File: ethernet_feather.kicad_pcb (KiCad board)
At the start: 4 copper layers, 48 parts, among them J1 USB_C_Receptacle_USB2.0, J2 TC2030-NL, J3 Conn_01x02_MountingPin, J4 RJ45_Abracon_ARJM11D7-114-AB-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, J5 Conn_02x02_Odd_Even, U1 MIMXRT1051CVJ5B, U2 LP3982IMM-3.3, U3 MCP73831-2-OT, U4 W25Q32JVZP, U5 WE-TVS-82400102, Y1 24MHz 6pF, Y2 32.768kHz 7pF

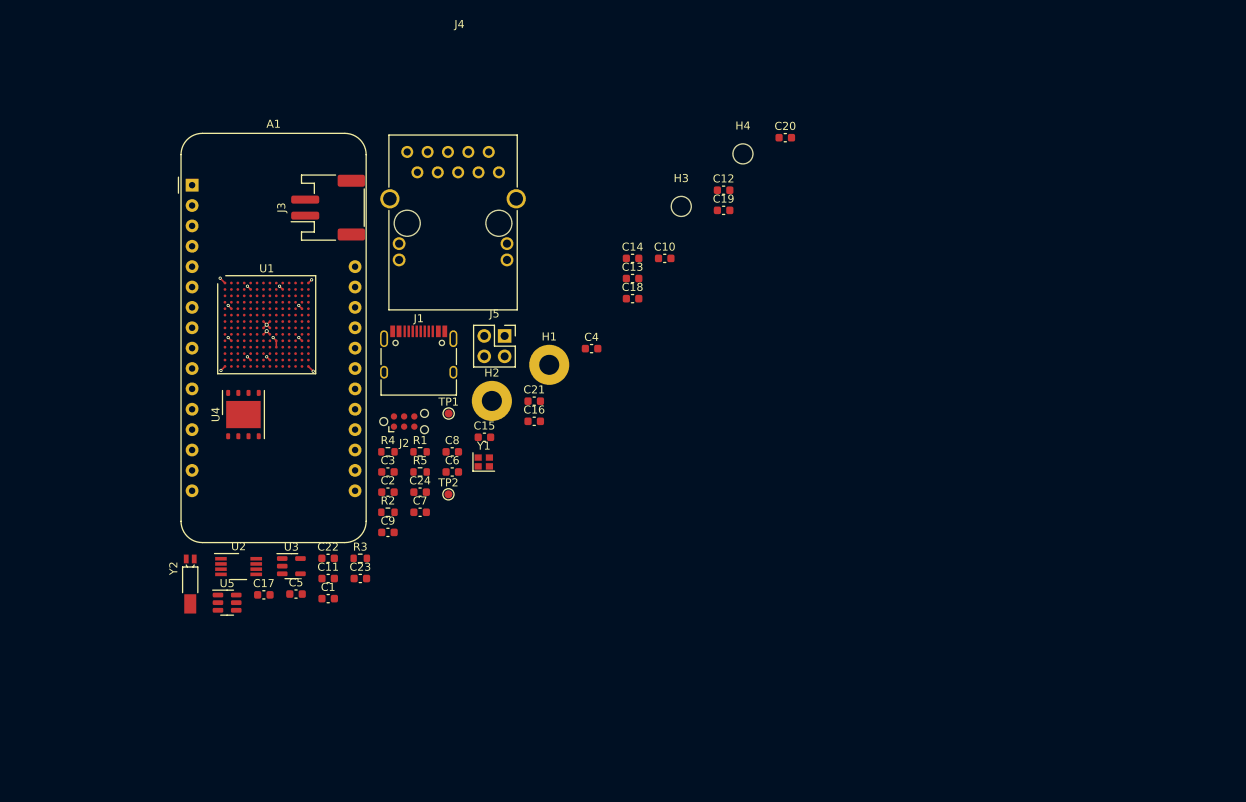
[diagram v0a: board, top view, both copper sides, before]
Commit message: Add microSD card and annotate mostly complete schematic
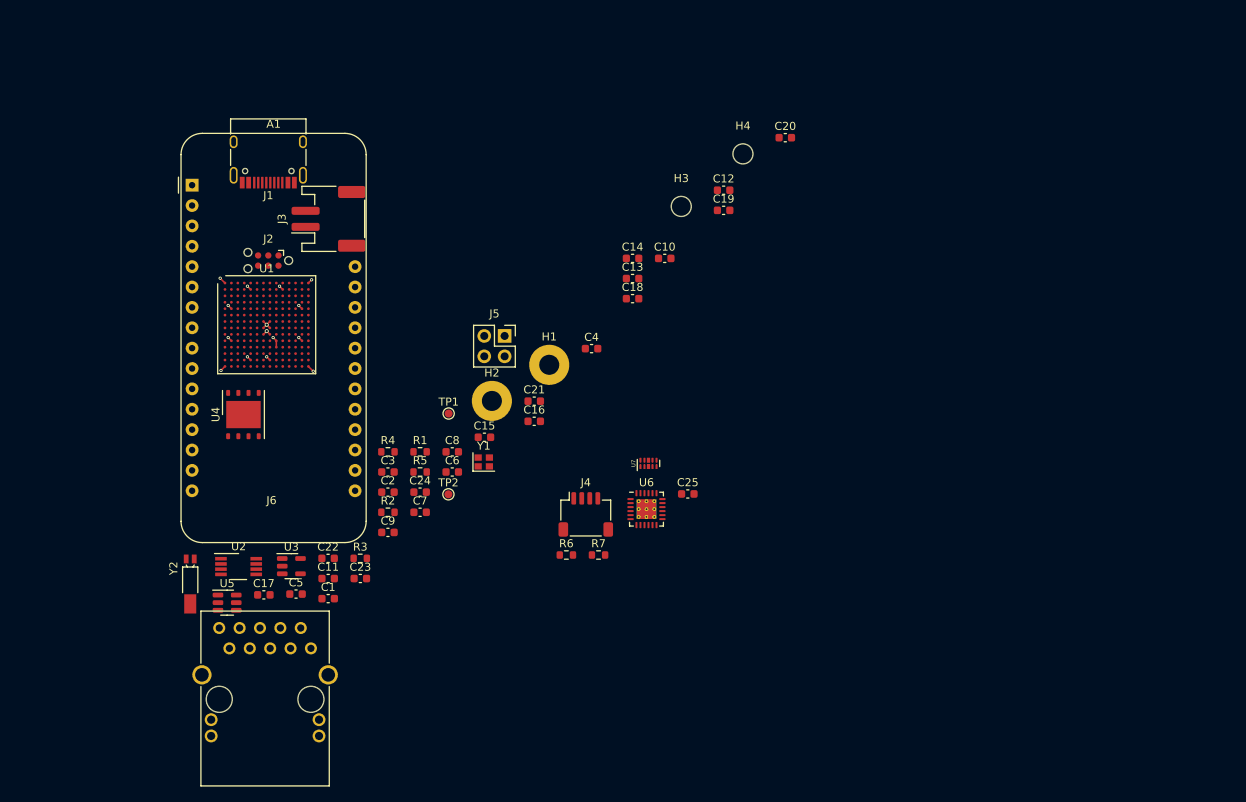
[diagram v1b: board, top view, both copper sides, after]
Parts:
- added C25: 100nF, Capacitor_SMD:C_0603_1608Metric, F.Cu at (151.6, 113.2)
- added J4: JST SH4 pin, Connector_JST:JST_SH_SM04B-SRSS-TB_1x04-1MP_P1.00mm_Horizontal, F.Cu at (138.9, 115.8)
- added R6: 10kΩ, Resistor_SMD:R_0603_1608Metric, F.Cu at (136.5, 120.8)
- added R7: 10kΩ, Resistor_SMD:R_0603_1608Metric, F.Cu at (140.5, 120.8)
- added U6: LAN8742A, Package_DFN_QFN:VQFN-24-1EP_4x4mm_P0.5mm_EP2.45x2.45mm_ThermalVias, F.Cu at (146.4, 115.1)
- added U7: HSP061-4M10, ethernet_feather:ST_µQFN-10L, F.Cu at (146.7, 109.4)
- J3: value Conn_01x02_MountingPin -> JST PH 2 pin
- moved J6 63.8 mm to (98.9, 138.8)
- moved J1 32.6 mm to (99.3, 70.3), turned to 180 degrees
- moved J2 26.3 mm to (99.3, 84.1), turned to 180 degrees
- moved J3 1.40 mm to (106.8, 78.9)
- renumbered J4 to J6
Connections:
- A1 pad 1: unconnected-(A1-Pad1) -> (no net)
- A1 pad 10: unconnected-(A1-Pad10) -> (no net)
- A1 pad 11: unconnected-(A1-Pad11) -> (no net)
- A1 pad 12: unconnected-(A1-Pad12) -> (no net)
- A1 pad 13: unconnected-(A1-Pad13) -> (no net)
- A1 pad 14: unconnected-(A1-Pad14) -> (no net)
- A1 pad 15: unconnected-(A1-Pad15) -> (no net)
- A1 pad 16: unconnected-(A1-Pad16) -> (no net)
- A1 pad 17: unconnected-(A1-Pad17) -> (no net)
- A1 pad 18: unconnected-(A1-Pad18) -> (no net)
- A1 pad 19: unconnected-(A1-Pad19) -> (no net)
- A1 pad 2: unconnected-(A1-Pad2) -> (no net)
- A1 pad 20: unconnected-(A1-Pad20) -> (no net)
- A1 pad 21: unconnected-(A1-Pad21) -> (no net)
- A1 pad 22: unconnected-(A1-Pad22) -> (no net)
- A1 pad 23: unconnected-(A1-Pad23) -> (no net)
- A1 pad 24: unconnected-(A1-Pad24) -> (no net)
- A1 pad 25: unconnected-(A1-Pad25) -> (no net)
- A1 pad 26: unconnected-(A1-Pad26) -> (no net)
- A1 pad 27: unconnected-(A1-Pad27) -> (no net)
- A1 pad 28: unconnected-(A1-Pad28) -> (no net)
- A1 pad 3: unconnected-(A1-Pad3) -> (no net)
- A1 pad 4: unconnected-(A1-Pad4) -> (no net)
- A1 pad 5: unconnected-(A1-Pad5) -> (no net)
- A1 pad 6: unconnected-(A1-Pad6) -> (no net)
- A1 pad 7: unconnected-(A1-Pad7) -> (no net)
- A1 pad 8: unconnected-(A1-Pad8) -> (no net)
- A1 pad 9: unconnected-(A1-Pad9) -> (no net)
- C5 pad 1: unconnected-(C5-Pad1) -> (no net)
- C5 pad 2: unconnected-(C5-Pad2) -> (no net)
- J1 pad A8: unconnected-(J1-PadA8) -> (no net)
- J1 pad B8: unconnected-(J1-PadB8) -> (no net)
- J2 pad 4: /SWCLK -> (no net)
- J6 pad 10: unconnected-(J4-Pad10) -> /ENET_TX+
- J6 pad 11: unconnected-(J4-Pad11) -> (no net)
- J6 pad 12: unconnected-(J4-Pad12) -> (no net)
- J6 pad 13: unconnected-(J4-Pad13) -> (no net)
- J6 pad 14: unconnected-(J4-Pad14) -> (no net)
- J6 pad 3: unconnected-(J4-Pad3) -> /ENET_RX-
- J6 pad 5: unconnected-(J4-Pad5) -> /ENET_RX+
- J6 pad 8: unconnected-(J4-Pad8) -> /ENET_TX-
- U1 pad A11: unconnected-(U1-PadA11) -> (no net)
- U1 pad A12: unconnected-(U1-PadA12) -> (no net)
- U1 pad A13: unconnected-(U1-PadA13) -> (no net)
- U1 pad A2: unconnected-(U1-PadA2) -> (no net)
- U1 pad A3: unconnected-(U1-PadA3) -> (no net)
- U1 pad A4: unconnected-(U1-PadA4) -> (no net)
- U1 pad A5: unconnected-(U1-PadA5) -> (no net)
- U1 pad A6: unconnected-(U1-PadA6) -> (no net)
- U1 pad A7: unconnected-(U1-PadA7) -> (no net)
- U1 pad A9: /SWDCLK -> (no net)
- U1 pad B1: unconnected-(U1-PadB1) -> (no net)
- U1 pad B11: unconnected-(U1-PadB11) -> (no net)
- U1 pad B12: unconnected-(U1-PadB12) -> (no net)
- U1 pad B13: unconnected-(U1-PadB13) -> (no net)
- U1 pad B14: unconnected-(U1-PadB14) -> (no net)
- U1 pad B2: unconnected-(U1-PadB2) -> (no net)
- U1 pad B3: unconnected-(U1-PadB3) -> (no net)
- U1 pad B4: unconnected-(U1-PadB4) -> (no net)
- U1 pad B6: unconnected-(U1-PadB6) -> (no net)
- U1 pad B7: unconnected-(U1-PadB7) -> (no net)
- U1 pad B8: unconnected-(U1-PadB8) -> (no net)
- U1 pad B9: unconnected-(U1-PadB9) -> (no net)
- U1 pad C1: unconnected-(U1-PadC1) -> (no net)
- U1 pad C10: unconnected-(U1-PadC10) -> (no net)
- U1 pad C11: unconnected-(U1-PadC11) -> (no net)
- U1 pad C12: unconnected-(U1-PadC12) -> (no net)
- U1 pad C13: unconnected-(U1-PadC13) -> (no net)
- U1 pad C14: unconnected-(U1-PadC14) -> (no net)
- U1 pad C2: unconnected-(U1-PadC2) -> (no net)
- U1 pad C3: unconnected-(U1-PadC3) -> (no net)
- U1 pad C4: unconnected-(U1-PadC4) -> (no net)
- U1 pad C5: unconnected-(U1-PadC5) -> (no net)
- U1 pad C6: unconnected-(U1-PadC6) -> (no net)
- U1 pad C7: unconnected-(U1-PadC7) -> (no net)
- U1 pad C8: unconnected-(U1-PadC8) -> (no net)
- U1 pad C9: unconnected-(U1-PadC9) -> (no net)
- U1 pad D1: unconnected-(U1-PadD1) -> (no net)
- U1 pad D11: unconnected-(U1-PadD11) -> (no net)
- U1 pad D12: unconnected-(U1-PadD12) -> (no net)
- U1 pad D13: unconnected-(U1-PadD13) -> (no net)
- U1 pad D14: unconnected-(U1-PadD14) -> (no net)
- U1 pad D2: unconnected-(U1-PadD2) -> (no net)
- U1 pad D3: unconnected-(U1-PadD3) -> (no net)
- U1 pad D4: unconnected-(U1-PadD4) -> (no net)
- U1 pad D5: unconnected-(U1-PadD5) -> (no net)
- U1 pad D6: unconnected-(U1-PadD6) -> (no net)
- U1 pad D7: unconnected-(U1-PadD7) -> (no net)
- U1 pad D8: unconnected-(U1-PadD8) -> (no net)
- U1 pad D9: unconnected-(U1-PadD9) -> (no net)
- U1 pad E1: unconnected-(U1-PadE1) -> (no net)
- U1 pad E10: unconnected-(U1-PadE10) -> (no net)
- U1 pad E11: unconnected-(U1-PadE11) -> (no net)
- U1 pad E12: unconnected-(U1-PadE12) -> (no net)
- U1 pad E14: unconnected-(U1-PadE14) -> (no net)
- U1 pad E3: unconnected-(U1-PadE3) -> (no net)
- U1 pad E4: unconnected-(U1-PadE4) -> (no net)
- U1 pad E5: unconnected-(U1-PadE5) -> (no net)
- U1 pad E7: unconnected-(U1-PadE7) -> (no net)
- U1 pad E8: unconnected-(U1-PadE8) -> (no net)
- U1 pad F1: unconnected-(U1-PadF1) -> (no net)
- U1 pad F11: unconnected-(U1-PadF11) -> (no net)
- U1 pad F12: unconnected-(U1-PadF12) -> (no net)
- U1 pad F13: unconnected-(U1-PadF13) -> (no net)
- U1 pad F14: unconnected-(U1-PadF14) -> (no net)
- U1 pad F2: unconnected-(U1-PadF2) -> (no net)
- U1 pad F3: unconnected-(U1-PadF3) -> (no net)
- U1 pad F4: unconnected-(U1-PadF4) -> (no net)
- U1 pad G1: unconnected-(U1-PadG1) -> (no net)
- U1 pad G10: unconnected-(U1-PadG10) -> (no net)
- U1 pad G11: unconnected-(U1-PadG11) -> (no net)
- U1 pad G12: unconnected-(U1-PadG12) -> (no net)
- U1 pad G13: unconnected-(U1-PadG13) -> (no net)
- U1 pad G14: unconnected-(U1-PadG14) -> (no net)
- U1 pad G2: unconnected-(U1-PadG2) -> (no net)
- U1 pad G3: unconnected-(U1-PadG3) -> (no net)
- U1 pad G4: unconnected-(U1-PadG4) -> (no net)
- U1 pad G5: unconnected-(U1-PadG5) -> (no net)
- U1 pad H1: unconnected-(U1-PadH1) -> (no net)
- U1 pad H10: unconnected-(U1-PadH10) -> (no net)
- U1 pad H11: unconnected-(U1-PadH11) -> (no net)
- U1 pad H12: unconnected-(U1-PadH12) -> (no net)
- U1 pad H13: unconnected-(U1-PadH13) -> (no net)
- U1 pad H14: unconnected-(U1-PadH14) -> (no net)
- U1 pad H2: unconnected-(U1-PadH2) -> (no net)
- U1 pad H3: unconnected-(U1-PadH3) -> (no net)
- U1 pad H4: unconnected-(U1-PadH4) -> (no net)
- U1 pad H5: unconnected-(U1-PadH5) -> (no net)
- U1 pad J1: unconnected-(U1-PadJ1) -> (no net)
- U1 pad J11: unconnected-(U1-PadJ11) -> (no net)
- U1 pad J12: unconnected-(U1-PadJ12) -> (no net)
- U1 pad J13: unconnected-(U1-PadJ13) -> (no net)
- U1 pad J14: unconnected-(U1-PadJ14) -> (no net)
- U1 pad J2: unconnected-(U1-PadJ2) -> (no net)
- U1 pad J3: unconnected-(U1-PadJ3) -> (no net)
- U1 pad J4: unconnected-(U1-PadJ4) -> (no net)
- U1 pad J5: unconnected-(U1-PadJ5) -> (no net)
- U1 pad K1: unconnected-(U1-PadK1) -> (no net)
- U1 pad K10: unconnected-(U1-PadK10) -> (no net)
- U1 pad K11: unconnected-(U1-PadK11) -> (no net)
- U1 pad K12: unconnected-(U1-PadK12) -> (no net)
- U1 pad K14: unconnected-(U1-PadK14) -> (no net)
- U1 pad K4: unconnected-(U1-PadK4) -> (no net)
- U1 pad K6: unconnected-(U1-PadK6) -> (no net)
- U1 pad K8: unconnected-(U1-PadK8) -> (no net)
- U1 pad L10: unconnected-(U1-PadL10) -> (no net)
- U1 pad L11: unconnected-(U1-PadL11) -> (no net)
- U1 pad L12: unconnected-(U1-PadL12) -> (no net)
- U1 pad L13: unconnected-(U1-PadL13) -> (no net)
- U1 pad L14: unconnected-(U1-PadL14) -> (no net)
- U1 pad L5: unconnected-(U1-PadL5) -> (no net)
- U1 pad L6: unconnected-(U1-PadL6) -> (no net)
- U1 pad L7: unconnected-(U1-PadL7) -> (no net)
- U1 pad M10: unconnected-(U1-PadM10) -> (no net)
- U1 pad M11: unconnected-(U1-PadM11) -> (no net)
- U1 pad M12: unconnected-(U1-PadM12) -> (no net)
- U1 pad M13: unconnected-(U1-PadM13) -> (no net)
- U1 pad M14: unconnected-(U1-PadM14) -> (no net)
- U1 pad M3: unconnected-(U1-PadM3) -> (no net)
- U1 pad M4: unconnected-(U1-PadM4) -> (no net)
- U1 pad M5: unconnected-(U1-PadM5) -> (no net)
- U1 pad M6: unconnected-(U1-PadM6) -> (no net)
- U1 pad M7: unconnected-(U1-PadM7) -> (no net)
- U1 pad M9: unconnected-(U1-PadM9) -> (no net)
- U1 pad N10: unconnected-(U1-PadN10) -> (no net)
- U1 pad N12: unconnected-(U1-PadN12) -> (no net)
- U1 pad N13: unconnected-(U1-PadN13) -> (no net)
- U1 pad N3: unconnected-(U1-PadN3) -> (no net)
- U1 pad N6: unconnected-(U1-PadN6) -> (no net)
- U1 pad P10: unconnected-(U1-PadP10) -> (no net)
- U1 pad P13: unconnected-(U1-PadP13) -> (no net)
- U1 pad P2: unconnected-(U1-PadP2) -> (no net)
- U1 pad P6: unconnected-(U1-PadP6) -> (no net)
- U1 pad P8: unconnected-(U1-PadP8) -> (no net)
- U2 pad 5: unconnected-(U2-Pad5) -> (no net)
- U3 pad 1: unconnected-(U3-Pad1) -> (no net)
- U3 pad 4: +5V -> (no net)

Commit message: YOU CAN'T CUT BACK ON DECOUPLING CAPACITORS! YOU WILL REGRET THIS!
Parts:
- removed A1: Adafruit_Feather_Generic, Module:Adafruit_Feather
- removed C1, C2: 2pF, Capacitor_SMD:C_0603_1608Metric
- removed C10, C8: 2.2µF, Capacitor_SMD:C_0603_1608Metric
- removed C11: 2.2nF, Capacitor_SMD:C_0603_1608Metric
- removed C12, C16, C19, C21: 4.7µF, Capacitor_SMD:C_0603_1608Metric
- removed C13, C14, C15, C17, C18, C20, C22, C23, C24, C25: 100nF, Capacitor_SMD:C_0603_1608Metric
- removed C3, C4: 4pF, Capacitor_SMD:C_0603_1608Metric
- removed C5: C_Small, Capacitor_SMD:C_0603_1608Metric
- removed C6: 220nF, Capacitor_SMD:C_0603_1608Metric
- removed C7: 1µF, Capacitor_SMD:C_0603_1608Metric
- removed C9: 33nF, Capacitor_SMD:C_0603_1608Metric
- removed H1, H2: 0.1", MountingHole:MountingHole_2.5mm_Pad
- removed H3, H4: 0.1", MountingHole:MountingHole_2.5mm
- removed J1: USB_C_Receptacle_USB2.0, Connector_USB:USB_C_Receptacle_HRO_TYPE-C-31-M-12
- removed J2: TC2030-NL, Connector:Tag-Connect_TC2030-IDC-NL_2x03_P1.27mm_Vertical
- removed J3: JST PH 2 pin, Connector_JST:JST_PH_S2B-PH-SM4-TB_1x02-1MP_P2.00mm_Horizontal
- removed J4: JST SH4 pin, Connector_JST:JST_SH_SM04B-SRSS-TB_1x04-1MP_P1.00mm_Horizontal
- removed J5: Conn_02x02_Odd_Even, Connector_PinSocket_2.54mm:PinSocket_2x02_P2.54mm_Vertical
- removed J6: RJ45_Abracon_ARJM11D7-114-AB-EW2, ethernet_feather:RJ45_Abracon_ARJM11D7-114
- removed R1, R2: 5.6kΩ, Resistor_SMD:R_0603_1608Metric
- removed R3: 100kΩ, Resistor_SMD:R_0603_1608Metric
- removed R4: 120kΩ, Resistor_SMD:R_0603_1608Metric
- removed R5, R6, R7: 10kΩ, Resistor_SMD:R_0603_1608Metric
- removed TP1: D-2, TestPoint:TestPoint_Pad_D1.0mm
- removed TP2: D+2, TestPoint:TestPoint_Pad_D1.0mm
- removed U1: MIMXRT1051CVJ5B, ethernet_feather:LFBGA-196_12x12mm_Layout14x14_P0.8mm
- removed U2: LP3982IMM-3.3, Package_SO:VSSOP-8_3.0x3.0mm_P0.65mm
- removed U3: MCP73831-2-OT, Package_TO_SOT_SMD:SOT-23-5
- removed U4: W25Q32JVZP, Package_SON:WSON-8-1EP_6x5mm_P1.27mm_EP3.4x4.3mm
- removed U5: WE-TVS-82400102, Package_TO_SOT_SMD:SOT-23-6
- removed U6: LAN8742A, Package_DFN_QFN:VQFN-24-1EP_4x4mm_P0.5mm_EP2.45x2.45mm_ThermalVias
- removed U7: HSP061-4M10, ethernet_feather:ST_µQFN-10L
- removed Y1: 24MHz 6pF, Crystal:Crystal_SMD_2016-4Pin_2.0x1.6mm
- removed Y2: 32.768kHz 7pF, Crystal:Crystal_SMD_MicroCrystal_MS3V-T1R
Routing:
- net GND: track 12.3 -> 0.00 mm, vias 15 -> 0
- removed copper zone on In1.Cu, net GND

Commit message: Start PCB
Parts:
- added A1: Adafruit_Feather_Generic, Module:Adafruit_Feather, F.Cu at (100.0, 75.2)
- added C1: 100nF, Capacitor_SMD:C_0402_1005Metric, F.Cu at (162.5, 79.4)
- added C10: 4.7µF, Capacitor_SMD:C_0402_1005Metric, F.Cu at (171.5, 68.9)
- added C11: 100nF, Capacitor_SMD:C_0402_1005Metric, F.Cu at (156.2, 85.4)
- added C12: 100nF, Capacitor_SMD:C_0402_1005Metric, F.Cu at (162.9, 77.4)
- added C13: 4.7µF, Capacitor_SMD:C_0402_1005Metric, F.Cu at (126.7, 115.6)
- added C14: 100nF, Capacitor_SMD:C_0402_1005Metric, F.Cu at (123.8, 116.7)
- added C15: 1µF, Capacitor_SMD:C_0402_1005Metric, F.Cu at (137.9, 130.2)
- added C16: 220nF, Capacitor_SMD:C_0402_1005Metric, F.Cu at (167.1, 72.9)
- added C17: 4.7µF, Capacitor_SMD:C_0402_1005Metric, F.Cu at (150.6, 92.2)
- added C18: 220nF, Capacitor_SMD:C_0402_1005Metric, F.Cu at (126.7, 113.6)
- added C19: 4.7µF, Capacitor_SMD:C_0402_1005Metric, F.Cu at (133.3, 108.1)
- added C2: 4.7µF, Capacitor_SMD:C_0402_1005Metric, F.Cu at (129.8, 110.1)
- added C20: 220nF, Capacitor_SMD:C_0402_1005Metric, F.Cu at (133.3, 106.2)
- added C21: 100nF, Capacitor_SMD:C_0402_1005Metric, F.Cu at (159.1, 83.0)
- added C22: 10µF, Capacitor_SMD:C_0402_1005Metric, F.Cu at (159.6, 81.0)
- added C23: 220nF, Capacitor_SMD:C_0402_1005Metric, F.Cu at (156.3, 83.4)
- added C24: 220nF, Capacitor_SMD:C_0402_1005Metric, F.Cu at (143.2, 98.2)
- added C25: 4.7µF, Capacitor_SMD:C_0402_1005Metric, F.Cu at (162.3, 116.7)
- added C26: 33µF, Capacitor_SMD:C_0402_1005Metric, F.Cu at (152.8, 87.7)
- added C27: 220nF, Capacitor_SMD:C_0402_1005Metric, F.Cu at (147.7, 92.2)
- added C28: 2.2µF, Capacitor_SMD:C_0402_1005Metric, F.Cu at (110.5, 81.0)
- added C29: 33nF, Capacitor_SMD:C_0402_1005Metric, F.Cu at (112.4, 84.7)
- added C3: 100nF, Capacitor_SMD:C_0402_1005Metric, F.Cu at (126.8, 111.7)
- added C30: 2.2µF, Capacitor_SMD:C_0402_1005Metric, F.Cu at (108.6, 81.0)
- added C31: 2.2nF, Capacitor_SMD:C_0402_1005Metric, F.Cu at (109.8, 85.7)
- added C32: 100nF, Capacitor_SMD:C_0402_1005Metric, F.Cu at (156.7, 81.0)
- added C33: 4pF, Capacitor_SMD:C_0402_1005Metric, F.Cu at (141.9, 122.7)
- added C34: 4pF, Capacitor_SMD:C_0402_1005Metric, F.Cu at (137.0, 105.7)
- added C35: 2pF, Capacitor_SMD:C_0402_1005Metric, F.Cu at (114.9, 101.3)
- added C36: 2pF, Capacitor_SMD:C_0402_1005Metric, F.Cu at (110.9, 103.8)
- added C37: 100nF, Capacitor_SMD:C_0402_1005Metric, F.Cu at (107.0, 113.7)
- added C38: 100nF, Capacitor_SMD:C_0402_1005Metric, F.Cu at (113.1, 114.3)
- added C39: 470pF, Capacitor_SMD:C_0402_1005Metric, F.Cu at (113.7, 108.2)
- added C4: 4.7µF, Capacitor_SMD:C_0402_1005Metric, F.Cu at (152.8, 89.7)
- added C40: 100nF, Capacitor_SMD:C_0402_1005Metric, F.Cu at (216.8, 75.3)
- added C41: 100nF, Capacitor_SMD:C_0402_1005Metric, F.Cu at (103.0, 118.4)
- added C42: 1µF, Capacitor_SMD:C_0402_1005Metric, F.Cu at (113.7, 107.2)
- added C43: 2pF, Capacitor_SMD:C_0402_1005Metric, F.Cu at (114.6, 111.3)
- added C44: 2pF, Capacitor_SMD:C_0402_1005Metric, F.Cu at (113.7, 109.2)
- added C5: 100nF, Capacitor_SMD:C_0402_1005Metric, F.Cu at (142.9, 125.7)
- added C6: 100nF, Capacitor_SMD:C_0402_1005Metric, F.Cu at (137.9, 132.2)
- added C7: 4.7µF, Capacitor_SMD:C_0402_1005Metric, F.Cu at (171.5, 70.8)
- added C8: 100nF, Capacitor_SMD:C_0402_1005Metric, F.Cu at (165.8, 75.4)
- added C9: 100nF, Capacitor_SMD:C_0402_1005Metric, F.Cu at (139.9, 101.7)
- added D1: D_Schottky, Diode_SMD:D_SOD-323, F.Cu at (106.0, 80.5)
- added FB1: 470Ω @ 100MHz, Inductor_SMD:L_0603_1608Metric, F.Cu at (106.3, 114.9)
- added H1: 0.1", MountingHole:MountingHole_2.5mm, F.Cu at (162.4, 71.2)
- added H2: 0.1", MountingHole:MountingHole_2.5mm_Pad, F.Cu at (118.6, 71.3)
- added H3: 0.1", MountingHole:MountingHole_2.5mm_Pad, F.Cu at (101.8, 71.5)
- added H4: 0.1", MountingHole:MountingHole_2.5mm, F.Cu at (154.3, 76.2)
- added J1: JST PH 2 pin, Connector_JST:JST_PH_S2B-PH-SM4-TB_1x02-1MP_P2.00mm_Horizontal, F.Cu at (116.7, 79.6)
- added J2: JST SH4 pin, Connector_JST:JST_SH_SM04B-SRSS-TB_1x04-1MP_P1.00mm_Horizontal, B.Cu at (118.2, 79.5)
- added J3: Molex 1051620001, ethernet_feather:microSD_HC_Molex_1051620001, B.Cu at (111.4, 104.6)
- added J4: TC2030-NL, Connector:Tag-Connect_TC2030-IDC-NL_2x03_P1.27mm_Vertical, F.Cu at (103.5, 110.0)
- added J5: USB_C_Receptacle_USB2.0, Connector_USB:USB_C_Receptacle_HRO_TYPE-C-31-M-12, F.Cu at (110.0, 70.1)
- added J6: RJ45_Abracon_ARJM11D7-114-AB-EW2, ethernet_feather:RJ45_Abracon_ARJM11D7-114, F.Cu at (110.0, 130.7)
- added J7: 2x2 header, Connector_PinSocket_2.54mm:PinSocket_2x02_P2.54mm_Vertical, B.Cu at (108.9, 129.8)
- added JP1: SolderJumper_3_Bridged123, ethernet_feather:SolderJumper-3_P1.3mm_Bridged123_RoundedPad1.0x1.5mm, B.Cu at (116.1, 85.1)
- added L1: 4.7µH, Inductor_SMD:L_0603_1608Metric, F.Cu at (173.9, 120.6)
- added Q1: Q_PMOS_DGS, Package_TO_SOT_SMD:SOT-23, F.Cu at (105.5, 77.5)
- added R1: 100kΩ, Resistor_SMD:R_0402_1005Metric, F.Cu at (106.0, 85.7)
- added R10: 10kΩ, Resistor_SMD:R_0402_1005Metric, F.Cu at (197.0, 92.5)
- added R11: 10kΩ, Resistor_SMD:R_0402_1005Metric, F.Cu at (194.1, 92.5)
- added R12: 10kΩ, Resistor_SMD:R_0402_1005Metric, F.Cu at (194.1, 94.5)
- added R13: 49.9Ω, Resistor_SMD:R_0402_1005Metric, F.Cu at (114.0, 117.7)
- added R14: 49.9Ω, Resistor_SMD:R_0402_1005Metric, F.Cu at (111.3, 118.5)
- added R15: 49.9Ω, Resistor_SMD:R_0402_1005Metric, F.Cu at (110.0, 117.2)
- added R16: 49.9Ω, Resistor_SMD:R_0402_1005Metric, F.Cu at (106.9, 117.6)
- added R17: 33Ω, Resistor_SMD:R_0402_1005Metric, F.Cu at (186.9, 103.7)
- added R18: 33Ω, Resistor_SMD:R_0402_1005Metric, F.Cu at (217.5, 68.9)
- added R19: 33Ω, Resistor_SMD:R_0402_1005Metric, F.Cu at (110.3, 105.5)
- added R2: 10kΩ, Resistor_SMD:R_0402_1005Metric, F.Cu at (130.4, 106.2)
- added R20: 33Ω, Resistor_SMD:R_0402_1005Metric, F.Cu at (207.2, 78.8)
- added R21: 12.1kΩ 1%, Resistor_SMD:R_0402_1005Metric, F.Cu at (113.6, 116.0)
- added R22: 10kΩ, Resistor_SMD:R_0402_1005Metric, F.Cu at (113.8, 112.5)
- added R23: 33Ω, Resistor_SMD:R_0402_1005Metric, F.Cu at (216.4, 71.4)
- added R24: 10kΩ, Resistor_SMD:R_0402_1005Metric, F.Cu at (189.9, 99.7)
- added R25: 270Ω, Resistor_SMD:R_0402_1005Metric, F.Cu at (119.7, 134.8)
- added R26: 270Ω, Resistor_SMD:R_0402_1005Metric, F.Cu at (100.3, 134.8)
- added R3: 120kΩ, Resistor_SMD:R_0402_1005Metric, F.Cu at (107.9, 85.7)
- added R4: 10kΩ, Resistor_SMD:R_0402_1005Metric, F.Cu at (116.7, 85.2)
- added R5: 10kΩ, Resistor_SMD:R_0402_1005Metric, F.Cu at (115.6, 85.2)
- added R6: 10kΩ, Resistor_SMD:R_0402_1005Metric, F.Cu at (109.0, 75.9)
- added R7: 5.1kΩ, Resistor_SMD:R_0402_1005Metric, B.Cu at (111.2, 70.8)
- added R8: 5.1kΩ, Resistor_SMD:R_0402_1005Metric, B.Cu at (108.2, 70.8)
- added R9: 1.5kΩ, Resistor_SMD:R_0402_1005Metric, F.Cu at (207.2, 80.8)
- added TP1: TestPoint, TestPoint:TestPoint_Pad_D1.0mm, B.Cu at (108.4, 85.6)
- added TP2: D-2, TestPoint:TestPoint_Pad_D1.0mm, F.Cu at (131.9, 99.1)
- added TP3: D+2, TestPoint:TestPoint_Pad_D1.0mm, F.Cu at (123.9, 110.2)
- added U1: MIMXRT1051CVJ5B, ethernet_feather:LFBGA-196_12x12mm_Layout14x14_P0.8mm, F.Cu at (110.0, 93.6)
- added U2: LP3982IMM-3.3, Package_SO:VSSOP-8_3.0x3.0mm_P0.65mm, F.Cu at (107.9, 83.3)
- added U3: MCP73831-2-OT, Package_TO_SOT_SMD:SOT-23-5, F.Cu at (109.5, 78.5)
- added U4: W25Q32JVZP, Package_SON:WSON-8-1EP_6x5mm_P1.27mm_EP3.4x4.3mm, F.Cu at (106.3, 103.7)
- added U5: WE-TVS-82400102, Package_TO_SOT_SMD:SOT-23-6, B.Cu at (109.5, 78.5)
- added U6: LAN8742A, Package_DFN_QFN:VQFN-24-1EP_4x4mm_P0.5mm_EP2.45x2.45mm_ThermalVias, F.Cu at (110.0, 110.6)
- added U7: HSP061-4M10, ethernet_feather:ST_µQFN-10L, F.Cu at (110.0, 114.7)
- added Y1: 32.768kHz, Crystal:Crystal_SMD_2520-4Pin_2.5x2.0mm, F.Cu at (132.6, 90.9)
- added Y2: 24MHz 6pF, Crystal:Crystal_SMD_2016-4Pin_2.0x1.6mm, F.Cu at (112.4, 101.9)
- added Y3: 25MHz, Crystal:Crystal_SMD_2016-4Pin_2.0x1.6mm, F.Cu at (116.6, 109.8)
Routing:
- net DCDC_GND: track 0.00 -> 58.9 mm, vias 0 -> 51
- net VUSB: track 0.00 -> 46.3 mm, vias 0 -> 4
- net Net-(J6-Pad13): track 0.00 -> 32.3 mm, vias 0 -> 1
- net Net-(J6-Pad11): track 0.00 -> 27.4 mm, vias 0 -> 1
- net NVCC_EMC: track 0.00 -> 21.9 mm, vias 0 -> 18
- net VBAT: track 0.00 -> 20.8 mm
- net /Ethernet/ENET_RX+: track 0.00 -> 20.6 mm
- net /Ethernet/ENET_RX-: track 0.00 -> 19.9 mm
- net /Ethernet/ENET_TX+: track 0.00 -> 16.6 mm
- net /Ethernet/ENET_TX-: track 0.00 -> 15.7 mm
- net Net-(C31-Pad1): track 0.00 -> 12.3 mm, vias 0 -> 2
- net Net-(J3-Pad7): track 0.00 -> 11.9 mm, vias 0 -> 1
- net VIN: track 0.00 -> 10.8 mm, vias 0 -> 2
- net /Ethernet/ENET_VDDA: track 0.00 -> 10.4 mm, vias 0 -> 7
- net Net-(J3-Pad8): track 0.00 -> 10.4 mm, vias 0 -> 1
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- added copper zone on In2.Cu, net /Ethernet/ENET_VDDA
- added copper zone on In1.Cu, net DCDC_GND
- added copper zone on In2.Cu, net NVCC_EMC
- added copper zone on In2.Cu, net VDD_SOC_IN
- added copper zone on In2.Cu, net VIN
